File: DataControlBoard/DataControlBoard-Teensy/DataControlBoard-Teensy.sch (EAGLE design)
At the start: 38 parts, among them IC1 74LS165D, IC2 74LS165D, J1 RS-Interface, J2 Pwr-Conn, J3 Static RPi, J4 Magnet RPi, J5 Boom Cam RPi, U1 MAX3232, U2 3V3REG

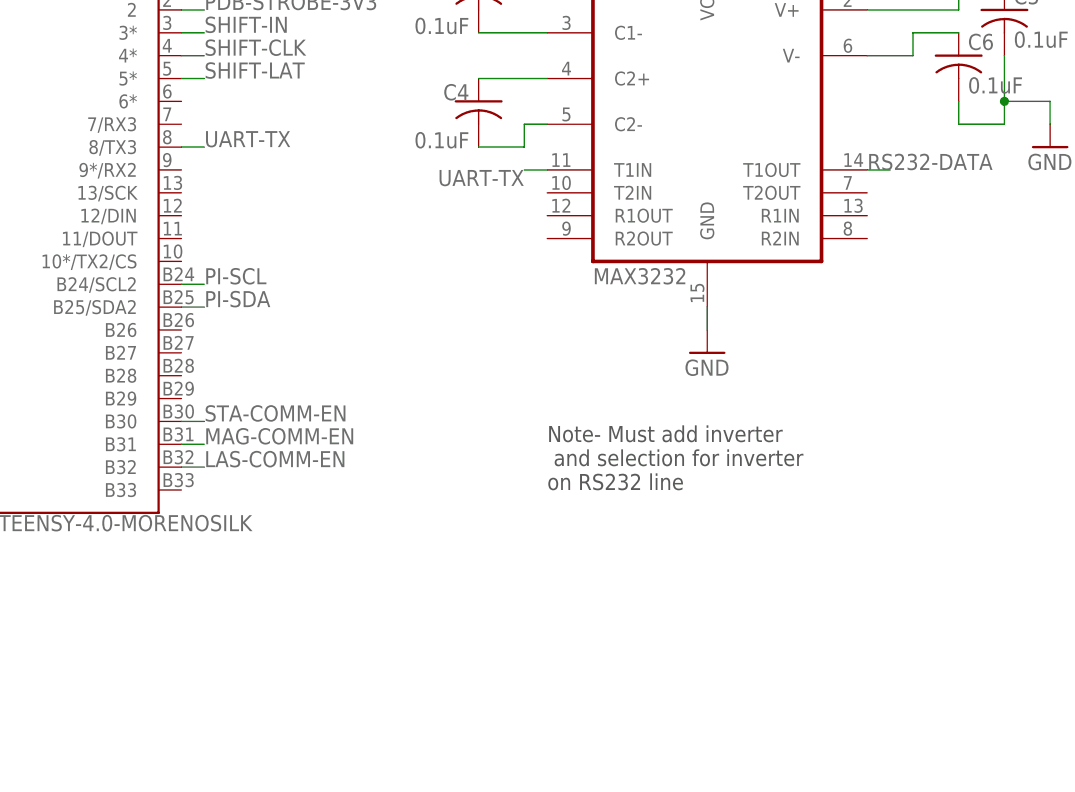
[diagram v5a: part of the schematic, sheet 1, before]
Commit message: Data control schem ready for double-check
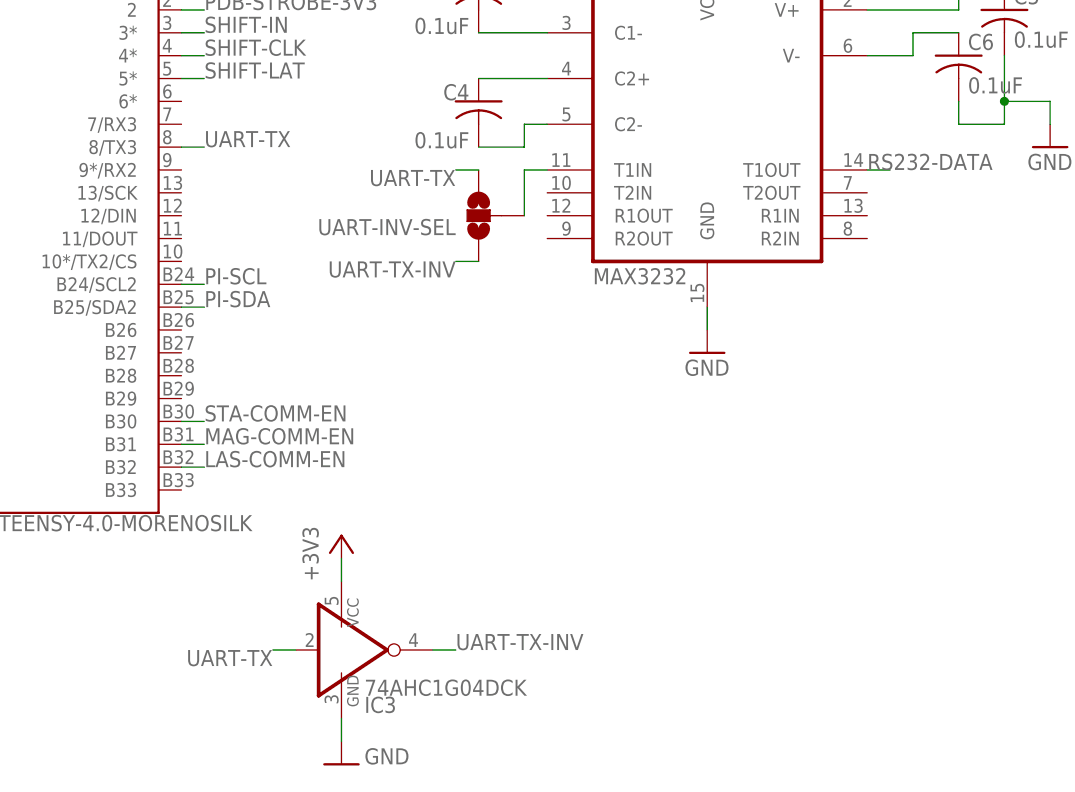
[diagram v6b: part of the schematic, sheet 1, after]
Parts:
- added IC3: 74AHC1G04DCK, 74xx-little-de:74AHC1G04DCK
- added UART-INV-SEL: JUMPER-SMT_3_NO_NO-SILK, SparkFun-Jumpers:JUMPER-SMT_3_NO_NO-SILK
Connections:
- new net N$20: U1.T1IN, UART-INV-SEL.2
- new net UART-TX-INV: IC3A.O, UART-INV-SEL.1
- net +3V3: now also IC3P.VCC
- net GND: now also IC3P.GND
- net UART-TX: now also IC3A.I, UART-INV-SEL.3; no longer U1.T1IN
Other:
- note removed: "Note- Must add inverter and selection for inverter on RS232 line"
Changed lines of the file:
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@@
 <part name="SDA-SEL3" library="SparkFun-Jumpers" library_urn="urn:adsk.eagle:library:528" deviceset="JUMPER-SMT_3_NO" device="_NO-SILK" package3d_urn="urn:adsk.eagle:package:39284/1"/>
 <part name="SCL-SEL3" library="SparkFun-Jumpers" library_urn="urn:adsk.eagle:library:528" deviceset="JUMPER-SMT_3_NO" device="_NO-SILK" package3d_urn="urn:adsk.eagle:package:39284/1"/>
+<part name="IC3" library="74xx-little-de" library_urn="urn:adsk.eagle:library:86" deviceset="74*1G04" device="DCK" package3d_urn="urn:adsk.eagle:package:2405/2" technology="AHC"/>
+<part name="UART-INV-SEL" library="SparkFun-Jumpers" library_urn="urn:adsk.eagle:library:528" deviceset="JUMPER-SMT_3_NO" device="_NO-SILK" package3d_urn="urn:adsk.eagle:package:39284/1"/>
+<part name="GND8" library="supply1" library_urn="urn:adsk.eagle:library:371" deviceset="GND" device=""/>
+<part name="+3V8" library="supply1" library_urn="urn:adsk.eagle:library:371" deviceset="+3V3" device=""/>
 </parts>
 <sheets>
@@
 <text x="167.64" y="35.56" size="1.778" layer="97" rot="R90" align="top-left">Level Shift
 from 5V to 3.3V</text>
-<text x="93.98" y="35.56" size="1.778" layer="97">Note- Must add inverter
- and selection for inverter
-on RS232 line</text>
 </plain>
 <instances>
@@
 <instance part="GND7" gate="1" x="149.86" y="73.66" smashed="yes">
 <attribute name="VALUE" x="147.32" y="71.12" size="1.778" layer="96"/>
+</instance>
+<instance part="IC3" gate="A" x="71.12" y="17.78" smashed="yes">
+<attribute name="NAME" x="73.66" y="10.795" size="1.778" layer="95"/>
+<attribute name="VALUE" x="73.66" y="12.7" size="1.778" layer="96"/>
+</instance>
+<instance part="IC3" gate="P" x="71.12" y="17.78" smashed="yes"/>
+<instance part="UART-INV-SEL" gate="G$1" x="86.36" y="66.04" smashed="yes" rot="R180">
+<attribute name="NAME" x="83.82" y="65.659" size="1.778" layer="95" font="vector" rot="R180"/>
+</instance>
+<instance part="GND8" gate="1" x="71.12" y="5.08" smashed="yes">
+<attribute name="VALUE" x="73.66" y="5.08" size="1.778" layer="96"/>
+</instance>
+<instance part="+3V8" gate="G$1" x="71.12" y="30.48" smashed="yes">
+<attribute name="VALUE" x="68.58" y="25.4" size="1.778" layer="96" rot="R90"/>
 </instance>
 </instances>
@@
 <junction x="144.78" y="78.74"/>
 </segment>
+<segment>
+<pinref part="IC3" gate="P" pin="GND"/>
+<pinref part="GND8" gate="1" pin="GND"/>
+<wire x1="71.12" y1="10.16" x2="71.12" y2="7.62" width="0.1524" layer="91"/>
+</segment>
 </net>
 <net name="PDB12" class="0">
@@
 <pinref part="U1" gate="G$1" pin="VCC"/>
 </segment>
+<segment>
+<wire x1="71.12" y1="25.4" x2="71.12" y2="27.94" width="0.1524" layer="91"/>
+<pinref part="+3V8" gate="G$1" pin="+3V3"/>
+<pinref part="IC3" gate="P" pin="VCC"/>
+</segment>
 </net>
 <net name="+5V" class="0">
@@
 </segment>
 <segment>
-<pinref part="U1" gate="G$1" pin="T1IN"/>
-<wire x1="93.98" y1="71.12" x2="91.44" y2="71.12" width="0.1524" layer="91"/>
-<label x="91.44" y="71.12" size="1.778" layer="95" rot="R180"/>
+<pinref part="IC3" gate="A" pin="I"/>
+<wire x1="66.04" y1="17.78" x2="63.5" y2="17.78" width="0.1524" layer="91"/>
+<label x="63.5" y="17.78" size="1.778" layer="95" rot="R180"/>
+</segment>
+<segment>
+<pinref part="UART-INV-SEL" gate="G$1" pin="3"/>
+<wire x1="86.36" y1="71.12" x2="83.82" y2="71.12" width="0.1524" layer="91"/>
+<label x="83.82" y="71.12" size="1.778" layer="95" rot="R180"/>
 </segment>
 </net>
@@
 </segment>
 </net>
+<net name="UART-TX-INV" class="0">
+<segment>
+<pinref part="IC3" gate="A" pin="O"/>
+<wire x1="81.28" y1="17.78" x2="83.82" y2="17.78" width="0.1524" layer="91"/>
+<label x="83.82" y="17.78" size="1.778" layer="95"/>
+</segment>
+<segment>
+<pinref part="UART-INV-SEL" gate="G$1" pin="1"/>
+<wire x1="86.36" y1="60.96" x2="83.82" y2="60.96" width="0.1524" layer="91"/>
+<label x="83.82" y="60.96" size="1.778" layer="95" rot="R180"/>
+</segment>
+</net>
+<net name="N$20" class="0">
+<segment>
+<pinref part="U1" gate="G$1" pin="T1IN"/>
+<wire x1="93.98" y1="71.12" x2="91.44" y2="71.12" width="0.1524" layer="91"/>
+<pinref part="UART-INV-SEL" gate="G$1" pin="2"/>
+<wire x1="91.44" y1="71.12" x2="91.44" y2="66.04" width="0.1524" layer="91"/>
+</segment>
+</net>

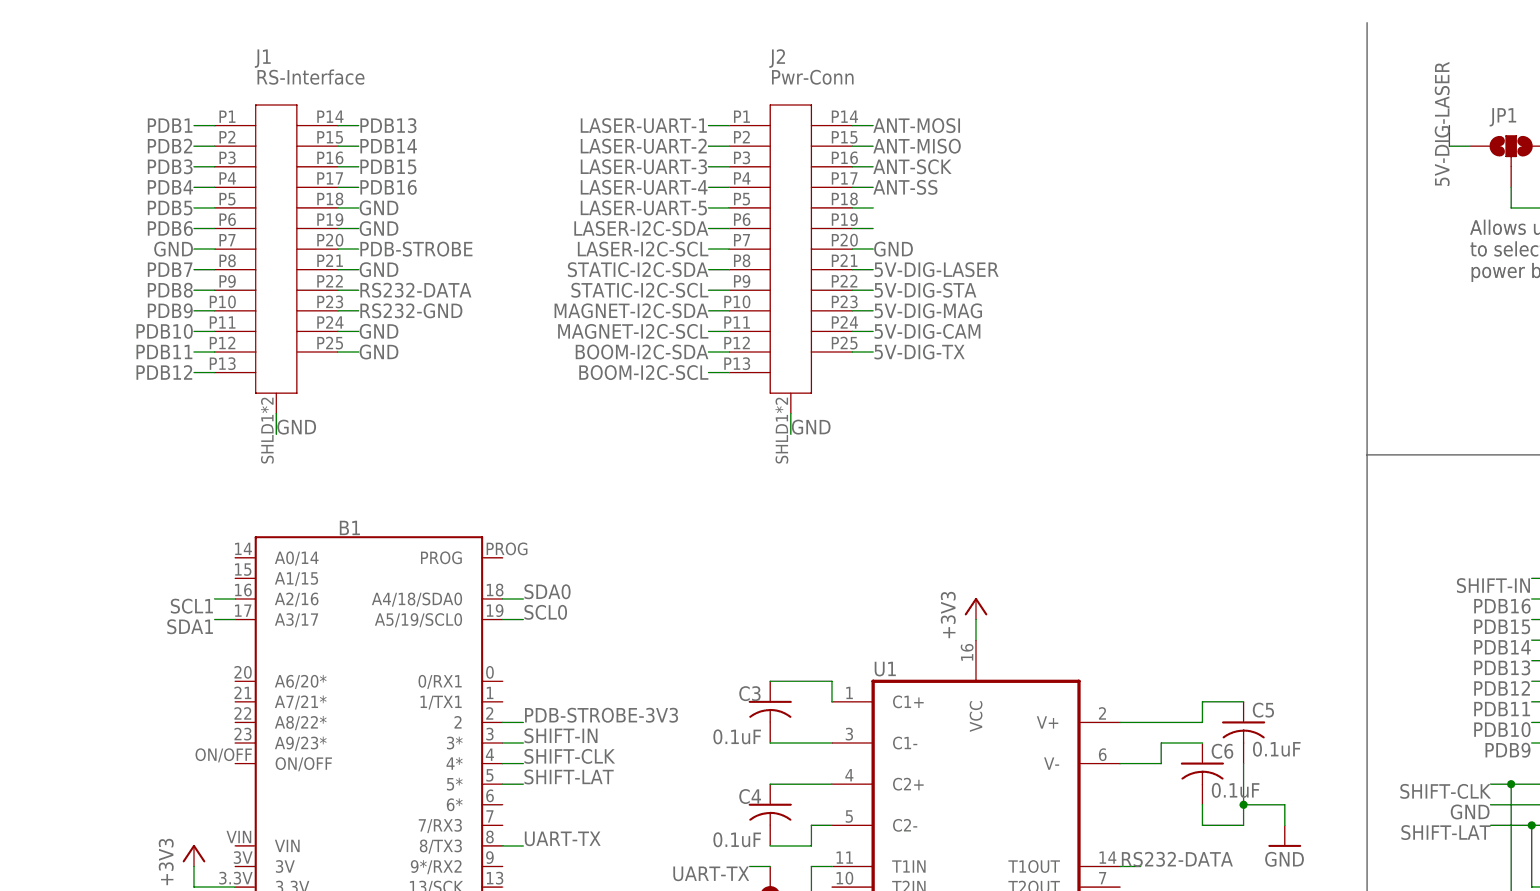
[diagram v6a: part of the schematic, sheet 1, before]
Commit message: Minor schematic changes, added GND merges and header for LIDAR
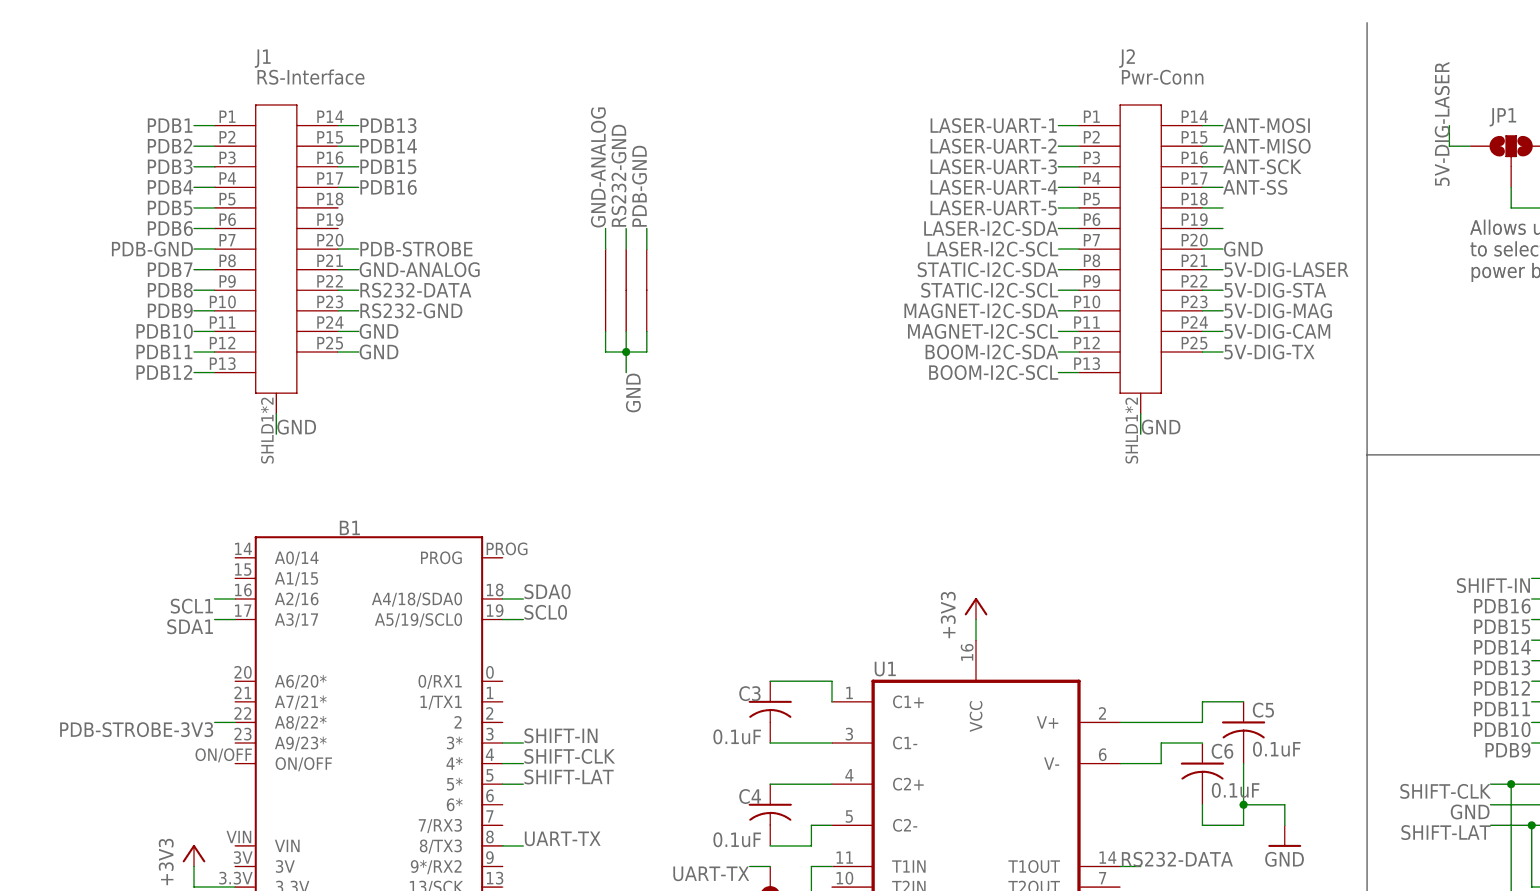
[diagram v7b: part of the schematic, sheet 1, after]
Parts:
- added J8: (no value), SparkFun-Connectors:CONN_07
- added U$1, U$2, U$3: GND-MERGER, RPi-Parts:GND-MERGER
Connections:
- new net DTR: J8.2
- new net GND-ANALOG: J1.P21, U$1.P$2
- new net PDB-GND: J1.P7, U$3.P$2
- new net RX: J8.5
- new net TX: J8.6
- new net VS: J8.4
- new net VS_2: J8.1
- net GND: now also J8.3, J8.7, U$1.P$1, U$2.P$1, U$3.P$1; no longer J1.P18, J1.P19, J1.P21, J1.P7
- net PDB-STROBE-3V3: now also B1.A8/22*; no longer B1.2
- net RS232-GND: now also U$2.P$2
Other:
- note added: "Connection header for RPi-LIDAR UART-USB converter Board"
- moved on the sheet: J2

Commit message: Significant routing progress
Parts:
- removed J3: Static RPi, SparkFun-Connectors:CONN_05X2PTH
- removed J4: Magnet RPi, SparkFun-Connectors:CONN_05X2PTH
- removed J5: Boom Cam RPi, SparkFun-Connectors:CONN_05X2PTH
- added J10: Magnet RPi, SparkFun-Connectors:CONN_05LOCK
- added J11: Boom Cam RPi, SparkFun-Connectors:CONN_05LOCK
- added J9: Static RPi, SparkFun-Connectors:CONN_05LOCK
- added TP10, TP11, TP12, TP13, TP14, TP15, TP16, TP17, TP18, TP19, TP20, TP8, TP9: TPPAD1-13, testpad:TPPAD1-13
- added TP4: GND, testpad:TPPAD1-13
- added TP5: 5V, testpad:TPPAD1-13
- added TP6: 3.3V, testpad:TPPAD1-13
- added TP7: STROBE, testpad:TPPAD1-13
- TP1, TP2, TP3: value TPPAD1-17 -> TPPAD1-13; device testpad:TPPAD1-17 -> testpad:TPPAD1-13
- renumbered JP1 to PWR-SEL
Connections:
- removed net DTR: J8.2
- removed net LASER-UART-1: J2.P1
- removed net LASER-UART-2: J2.P2
- removed net LASER-UART-3: J2.P3
- removed net LASER-UART-4: J2.P4
- removed net LASER-UART-5: J2.P5
- removed net N$15: J4.6
- removed net N$16: J4.8
- removed net N$17: J4.10
- removed net N$18: J3.5
- removed net N$19: J3.7
- removed net N$21: J3.2
- removed net N$22: J3.4
- removed net N$23: J3.6
- removed net N$24: J3.8
- removed net N$25: J3.10
- removed net RX: J8.5
- removed net TX: J8.6
- removed net VS: J8.4
- removed net VS_2: J8.1
- new net +3.3V: TP6.TP
- new net LASER-DTR: J2.P4, J8.2
- new net LASER-RX: J2.P2, J8.5
- new net LASER-TX: J2.P1, J8.6
- new net LASER-VS-1: J2.P3, J8.4
- new net LASER-VS-2: J2.P5, J8.1
- new net N$1: B1.0/RX1, TP12.TP
- new net N$12: B1.A7/21*, TP11.TP
- net +5V: now also TP5.TP
- net GND: now also TP4.TP
- net LAS-COMM-EN: now also J11.5; no longer J5.9
- net MAG-COMM-EN: now also J10.5; no longer J4.9
- net N$10: now also B1.A1/15, TP9.TP; no longer J5.8
- net N$11: now also B1.A6/20*, TP10.TP; no longer J5.10
- net N$13: now also B1.6*, TP19.TP; no longer J4.2
- net N$14: now also B1.7/RX3, TP20.TP; no longer J4.4
- net N$2: now also B1.1/TX1, TP13.TP; no longer J4.5
- net N$3: now also B1.2, TP14.TP; no longer J4.7
- net N$4: now also B1.9*/RX2, TP15.TP; no longer J5.5
- net N$5: now also B1.13/SCK, TP16.TP; no longer J5.7
- net N$7: now also B1.12/DIN, TP17.TP; no longer J5.2
- net N$8: now also B1.11/DOUT, TP18.TP; no longer J5.4
- net N$9: now also B1.A0/14, TP8.TP; no longer J5.6
- net PDB-STROBE: now also TP7.TP
- net PI-SCL: now also J10.2, J11.2, J9.2; no longer J3.3, J4.3, J5.3
- net PI-SDA: now also J10.1, J11.1, J9.1; no longer J3.1, J4.1, J5.1
- net STA-COMM-EN: now also J9.5; no longer J3.9
